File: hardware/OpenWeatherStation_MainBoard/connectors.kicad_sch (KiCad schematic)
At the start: 1 part, among them J2 Conn_01x05_Pin

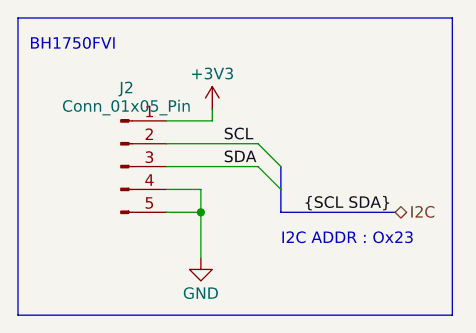
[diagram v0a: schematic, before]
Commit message: fix hierarchical bus
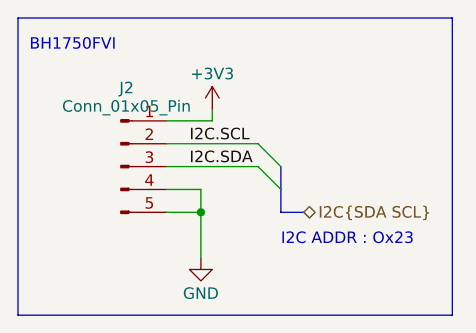
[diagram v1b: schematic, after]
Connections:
- net SCL renamed I2C.SCL
- net SDA renamed I2C.SDA
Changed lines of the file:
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@@
-    (stroke (width 0) (type default))
-  )
-  (bus (pts (xy 64.77 45.72) (xy 77.47 45.72))
     (stroke (width 0) (type default))
   )
   (wire (pts (xy 52.07 40.64) (xy 62.23 40.64))
+    (stroke (width 0) (type default))
+  )
+  (bus (pts (xy 64.77 45.72) (xy 67.31 45.72))
     (stroke (width 0) (type default))
   )
@@
     (effects (font (size 1.27 1.27)) (justify left bottom) (href "https://www.raspberryme.com/arduino-avec-capteur-de-lumiere-ambiante-bh1750/"))
   )
-  (label "SDA" (at 58.42 40.64 0) (fields_autoplaced)
+  (label "I2C.SDA" (at 54.61 40.64 0) (fields_autoplaced)
     (effects (font (size 1.27 1.27)) (justify left bottom))
   )
-  (label "{SCL SDA}" (at 67.31 45.72 0) (fields_autoplaced)
+  (label "I2C.SCL" (at 54.61 38.1 0) (fields_autoplaced)
     (effects (font (size 1.27 1.27)) (justify left bottom))
   )
-  (label "SCL" (at 58.42 38.1 0) (fields_autoplaced)
-    (effects (font (size 1.27 1.27)) (justify left bottom))
-  )
-  (hierarchical_label "I2C" (shape bidirectional) (at 77.47 45.72 0) (fields_autoplaced)
+  (hierarchical_label "I2C{SDA SCL}" (shape bidirectional) (at 67.31 45.72 0) (fields_autoplaced)
     (effects (font (size 1.27 1.27)) (justify left))
-    (property "SCL" "" (at 77.47 46.99 0)
+    (property "SCL" "" (at 67.31 46.99 0)
       (effects (font (size 1.27 1.27) italic) (justify left))
     )
-    (property "SDA" "" (at 77.47 48.4632 0)
+    (property "SDA" "" (at 67.31 48.4632 0)
       (effects (font (size 1.27 1.27) italic) (justify left))
     )

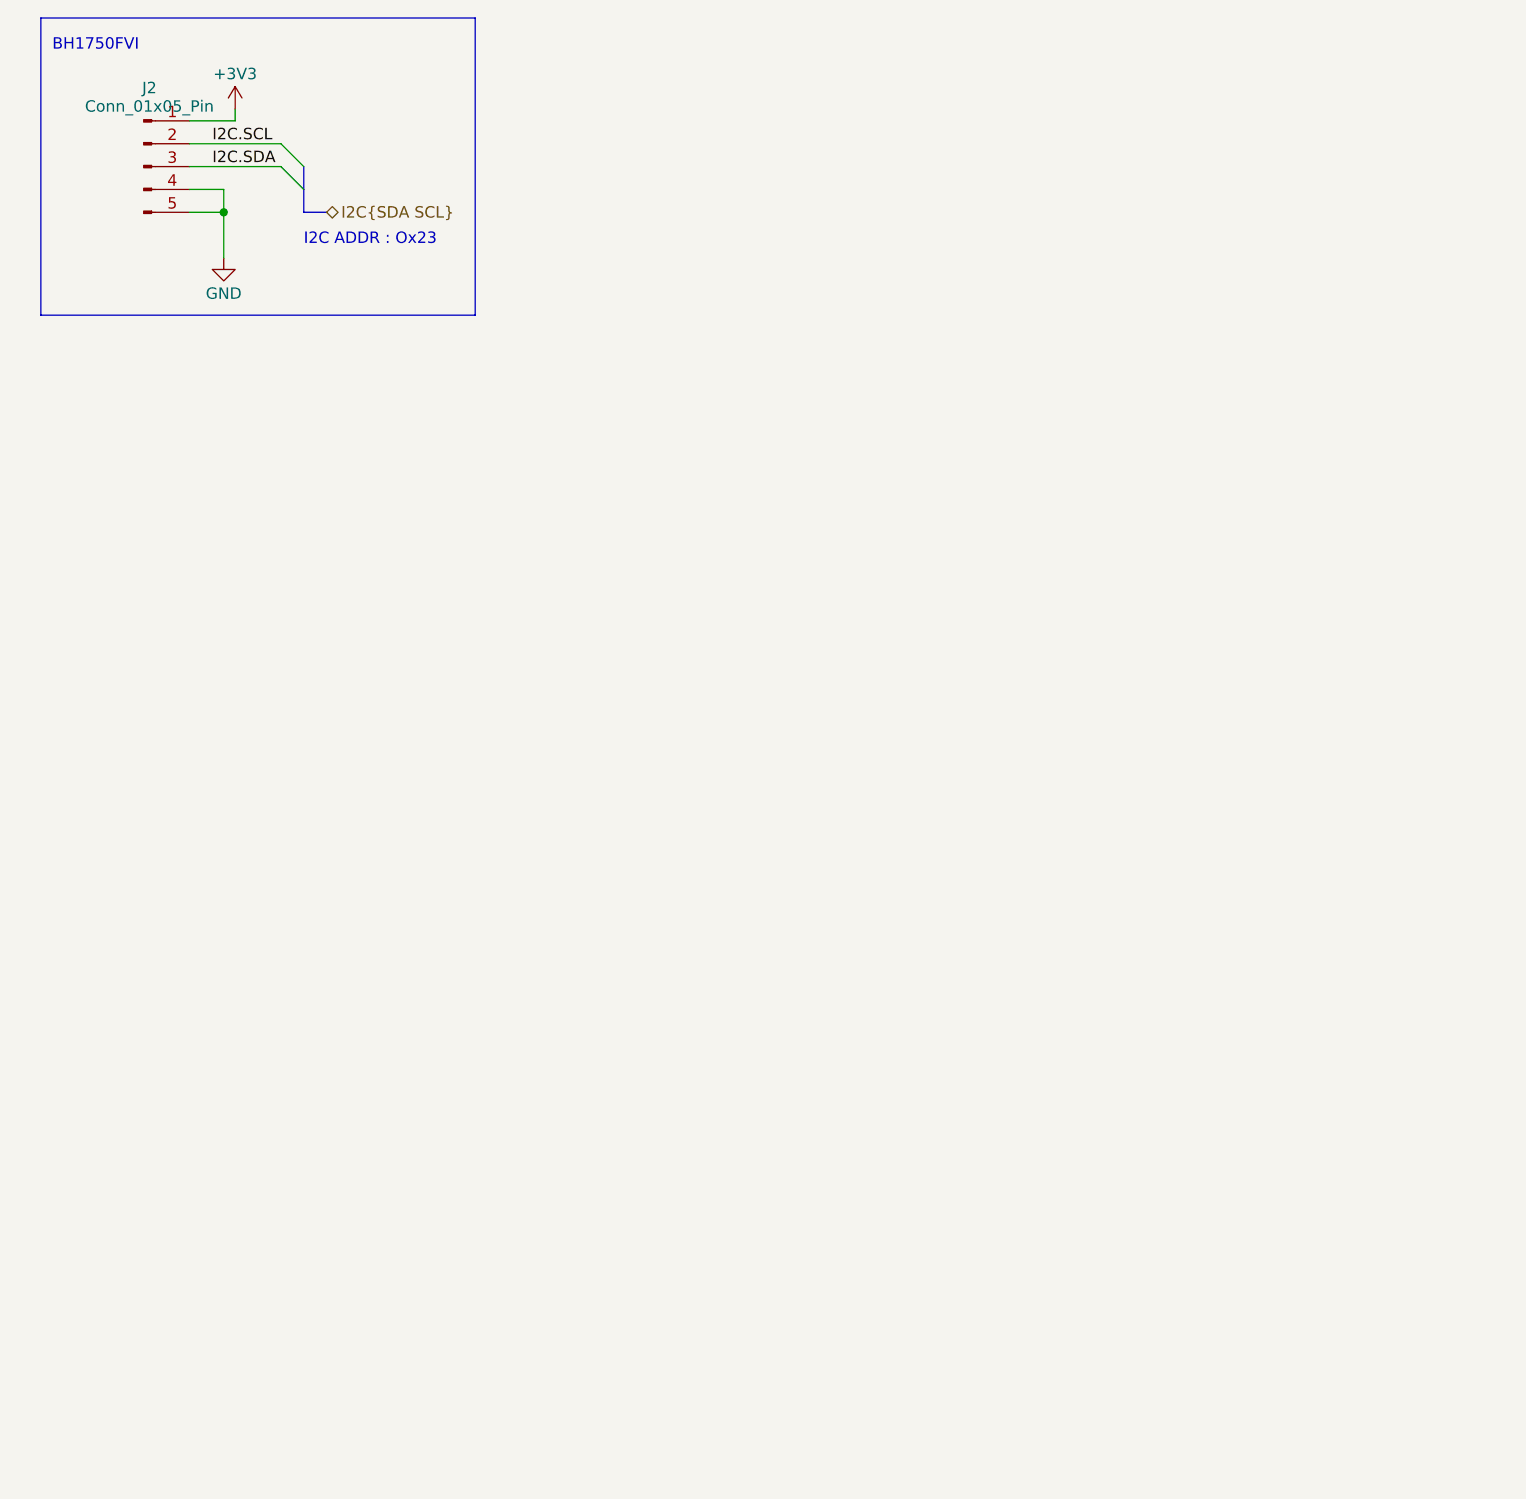
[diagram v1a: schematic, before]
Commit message: move eth connector to dedicated sheet
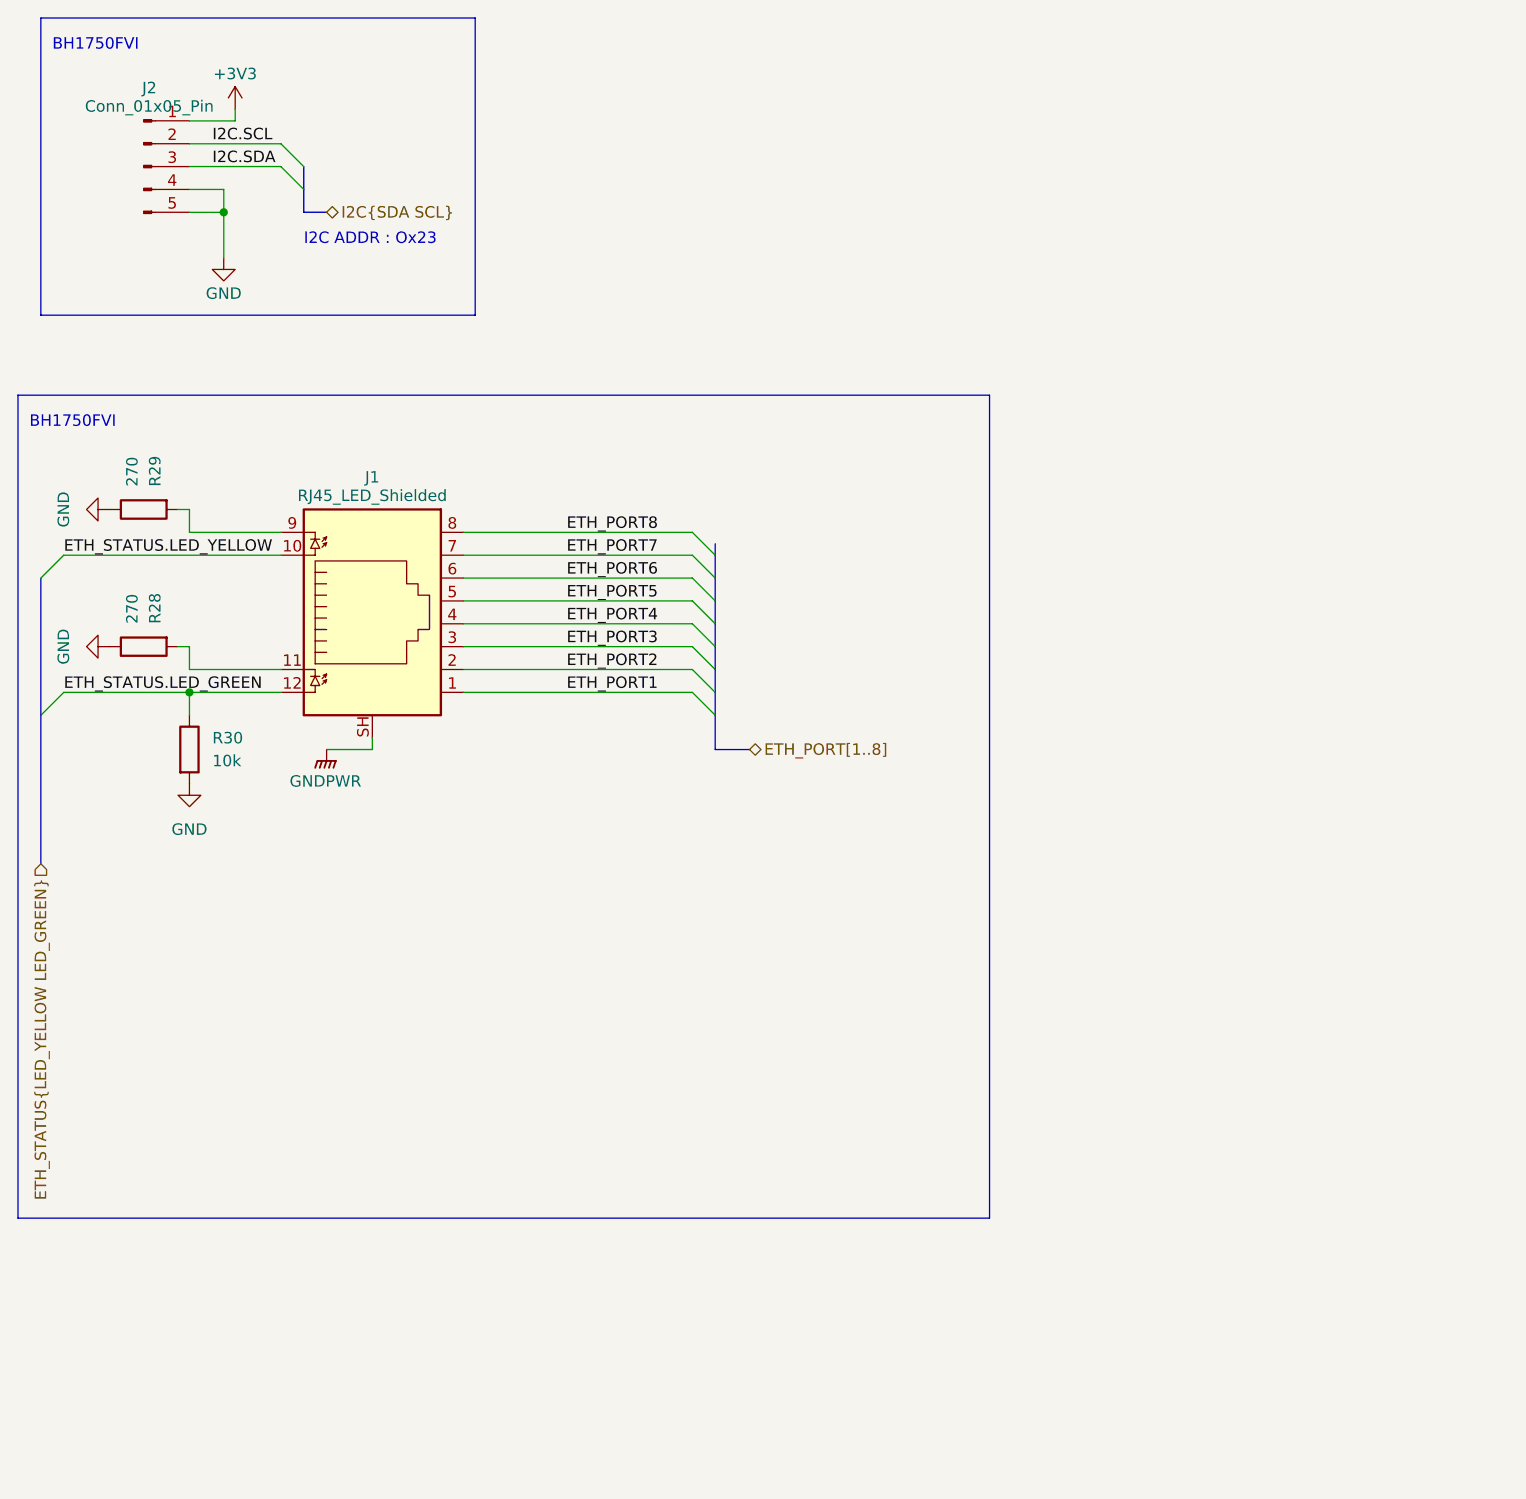
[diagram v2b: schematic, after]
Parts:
- added J1: RJ45_LED_Shielded, symbol Connector:RJ45_LED_Shielded
- added R28, R29: 270, symbol Device:R
- added R30: 10k, symbol Device:R
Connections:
- net GND: now also R28.1, R29.1, R30.2
- new net: J1.11, R28.2
- new net: J1.9, R29.2
- new net ETH_PORT1: J1.1
- new net ETH_PORT2: J1.2
- new net ETH_PORT3: J1.3
- new net ETH_PORT4: J1.4
- new net ETH_PORT5: J1.5
- new net ETH_PORT6: J1.6
- new net ETH_PORT7: J1.7
- new net ETH_PORT8: J1.8
- new net ETH_STATUS.LED_GREEN: J1.12, R30.1
- new net ETH_STATUS.LED_YELLOW: J1.10
- new net GNDPWR: J1.SH

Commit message: update schematics
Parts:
- added J4: Conn_02x07_Odd_Even, symbol Connector_Generic:Conn_02x07_Odd_Even
- added R28: 100, symbol Device:R
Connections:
- net +3V3: now also J4.3 (Pin_3)
- net GND: now also J4.5 (Pin_5), J4.7 (Pin_7), R28.1
- new net: J4.11 (Pin_11), R28.2
- new net SWD.NRST: J4.12 (Pin_12)
- new net SWD.SWCLK: J4.6 (Pin_6)
- new net SWD.SWDIO: J4.4 (Pin_4)
- new net SWD.SWO: J4.8 (Pin_8)
- new net VCP.RX: J4.13 (Pin_13)
- new net VCP.TX: J4.14 (Pin_14)
- no-connect marks 0 -> 4
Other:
- note added: "SWD Connector"

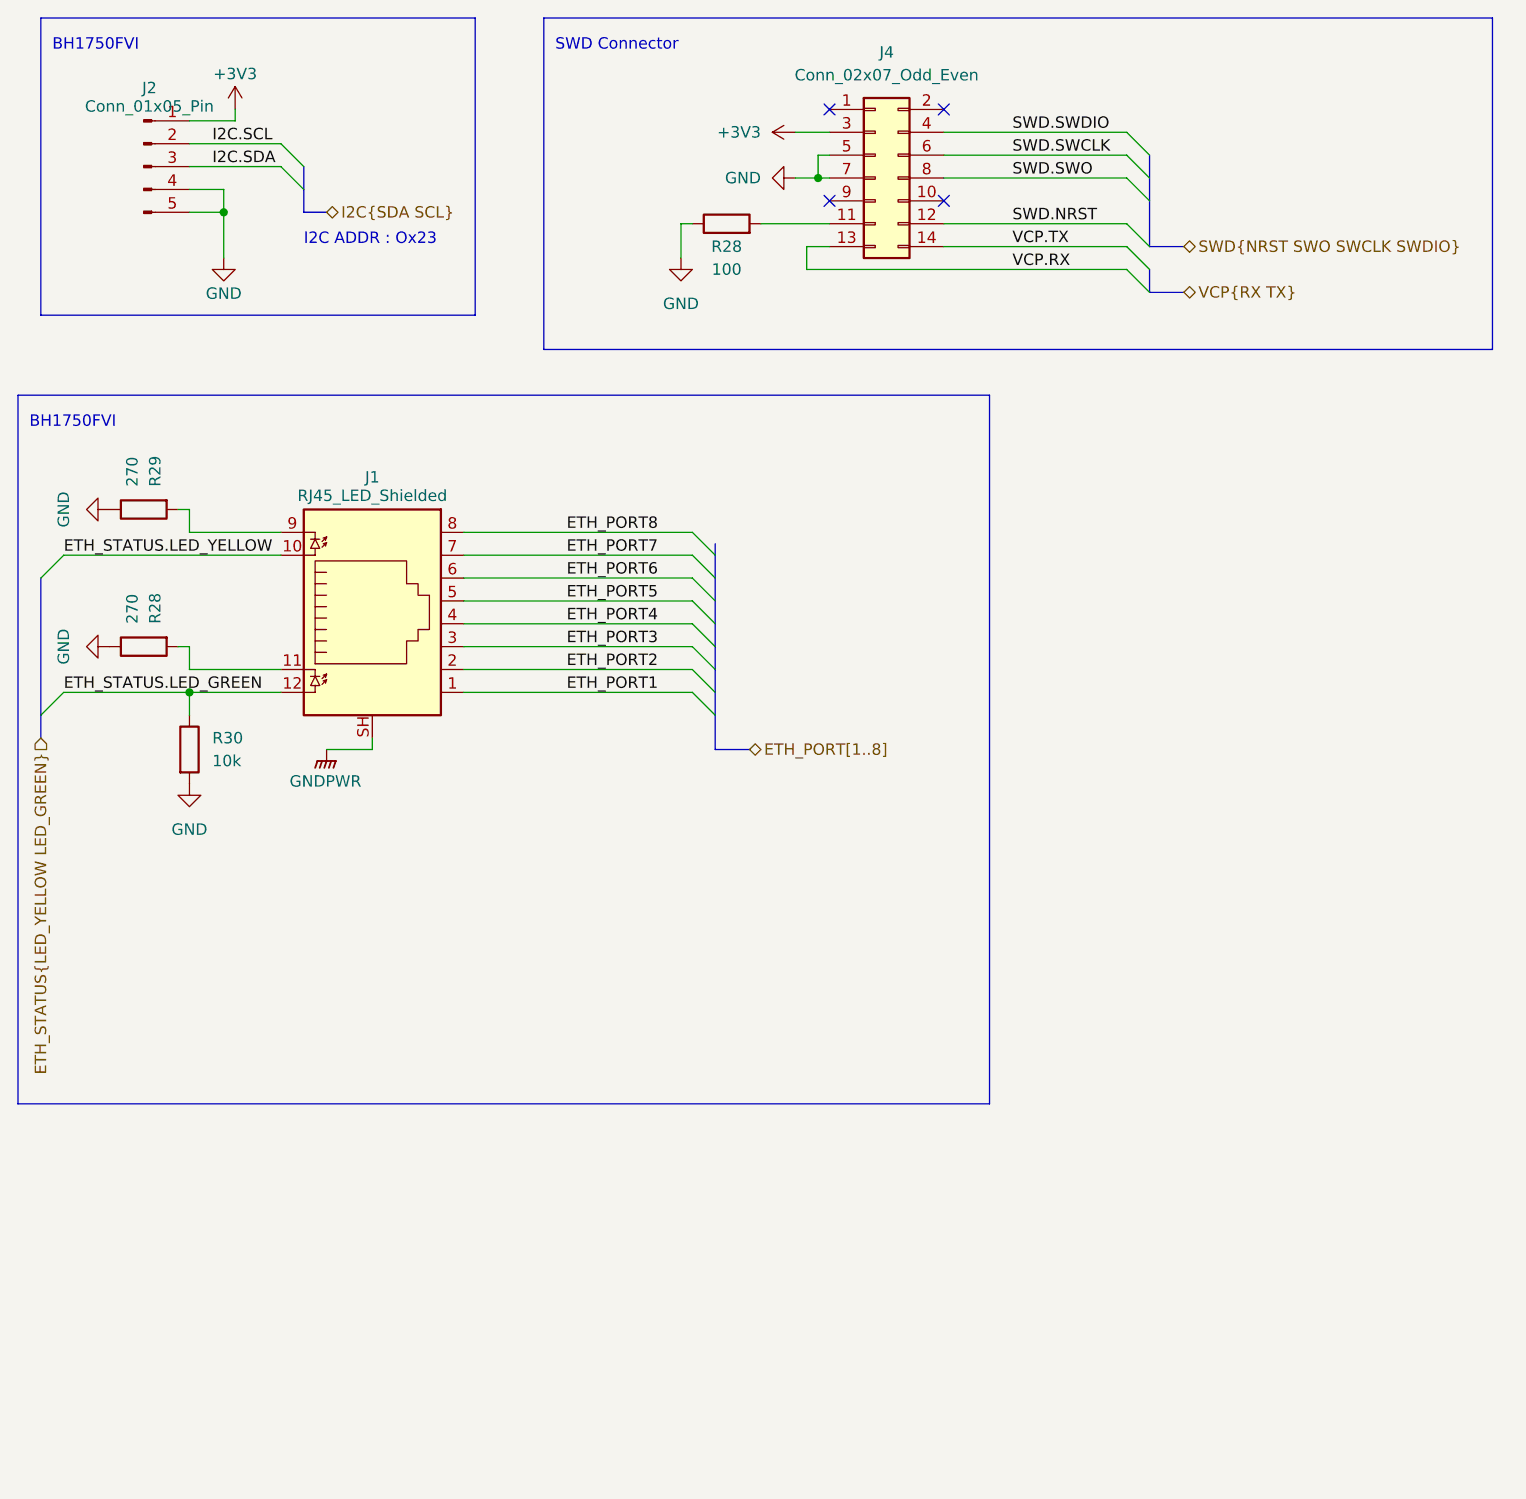
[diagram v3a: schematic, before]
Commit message: schematic update
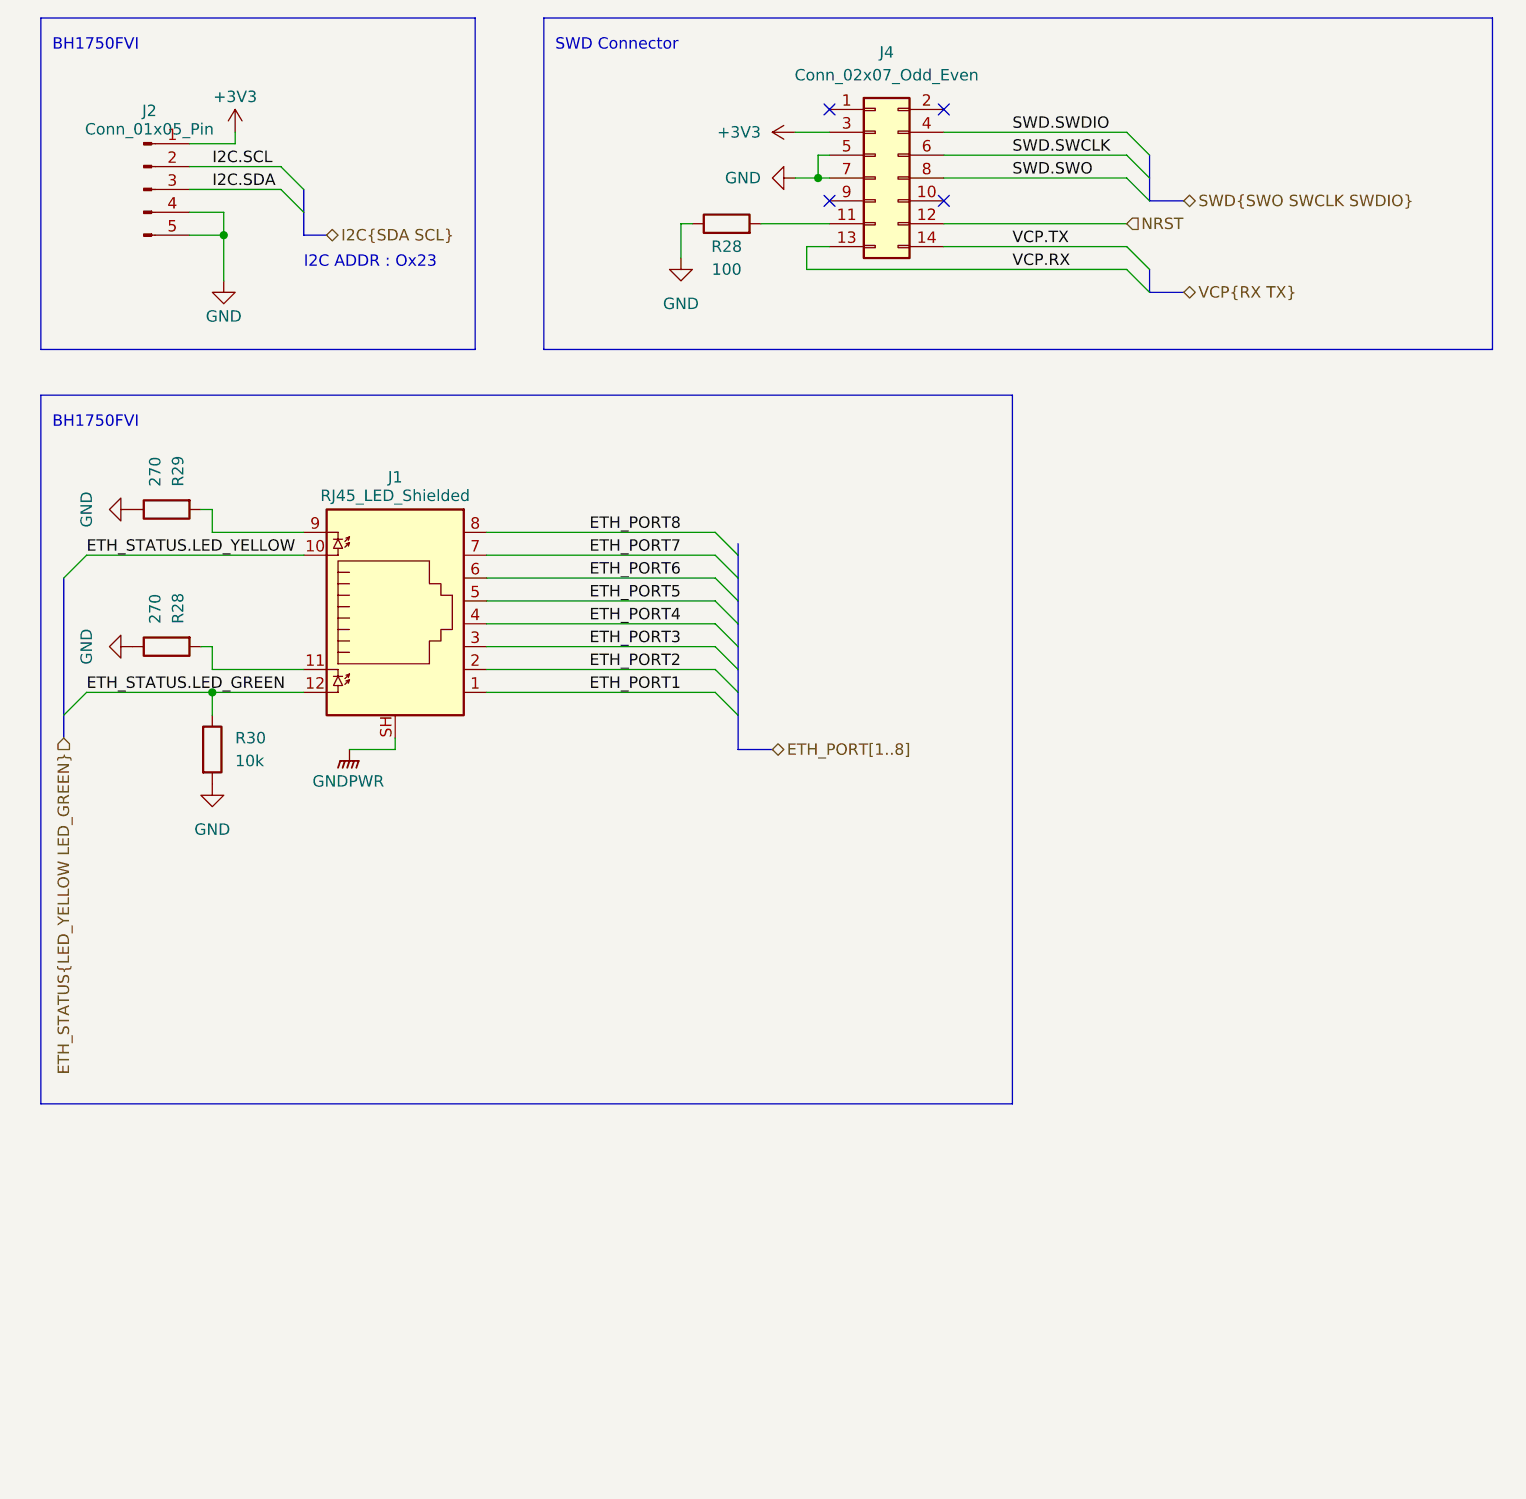
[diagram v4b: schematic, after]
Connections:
- net SWD.NRST renamed NRST
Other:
- moved on the sheet: J1, J2, R28, R29, R30
